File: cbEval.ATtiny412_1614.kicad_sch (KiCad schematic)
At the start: 59 parts, among them J1 Bergstik-II_3, J11 Bergstik-II_3, J12 Bergstik-II_3, J13 Bergstik-II_6, J14 Bergstik-II_6, J15 Bergstik-II_6, J16 Bergstik-II_3, J17 Bergstik-II_6, J18 Bergstik-II_3, J19 Bergstik-II_6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

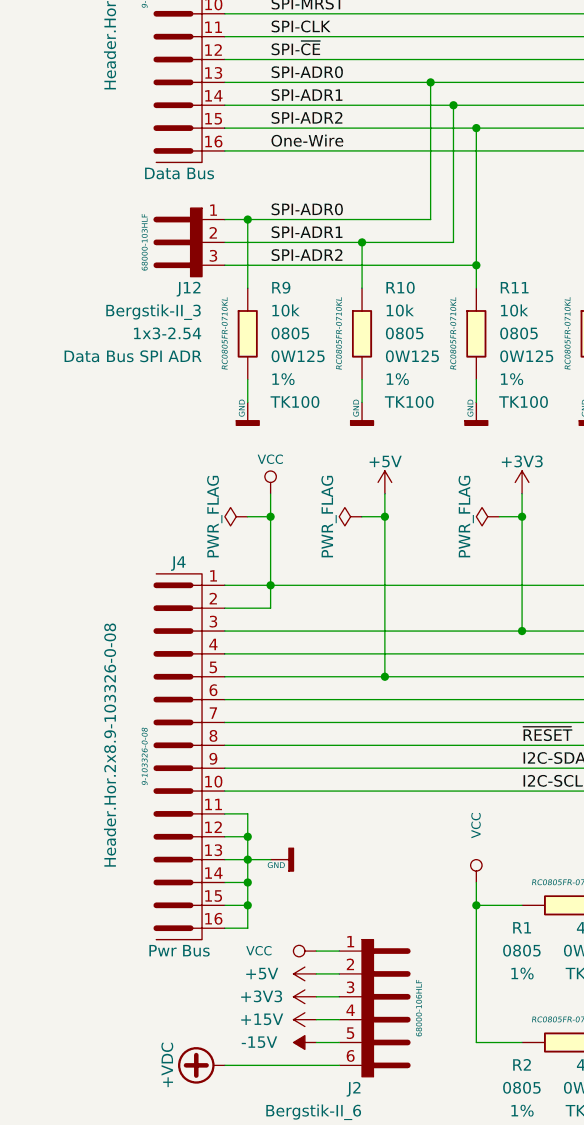
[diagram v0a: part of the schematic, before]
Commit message: Leiterplatte verkleinert, SilkScreen einiger Stecker verändert
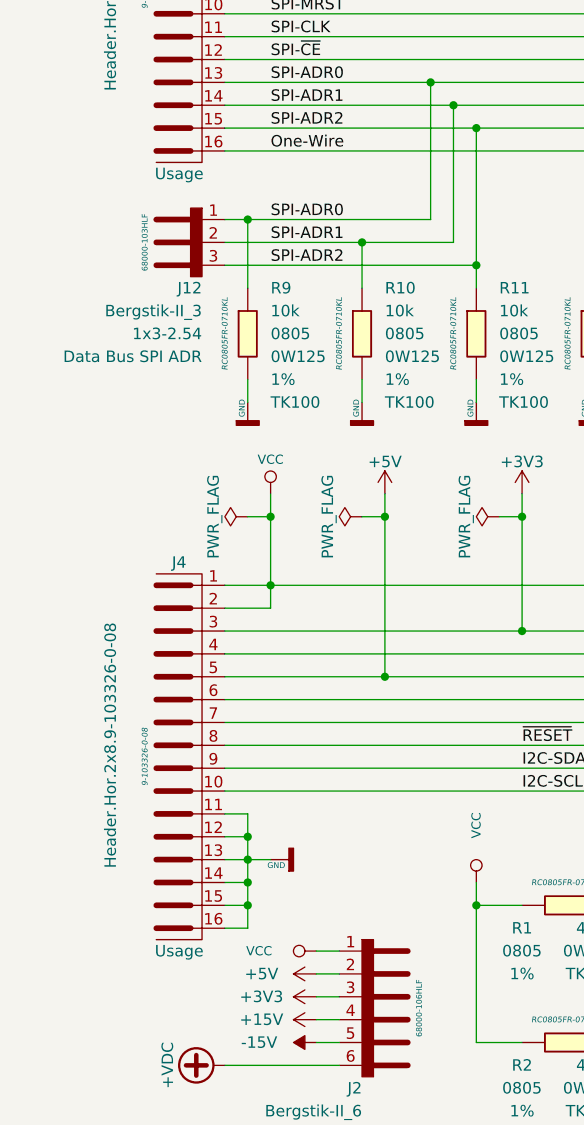
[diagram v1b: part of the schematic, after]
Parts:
- J3: footprint Connector_PinHeader_2.54mm:PinHeader_2x08_P2.54mm_Horizontal -> BTech.PinHeader.2-54mm:PinHeader_2x08_P2.54mm_Horizontal; Usage Data Bus -> Usage
- J4: footprint Connector_PinHeader_2.54mm:PinHeader_2x08_P2.54mm_Horizontal -> BTech.PinHeader.2-54mm:PinHeader_2x08_P2.54mm_Horizontal; Usage Pwr Bus -> Usage
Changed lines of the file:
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@@
     (property "Reference" "J4" (id 0) (at 27.94 129.54 0))
     (property "Value" "Header.Hor.2x8.9-103326-0-08" (id 1) (at 20.32 149.86 90))
-    (property "Footprint" "Connector_PinHeader_2.54mm:PinHeader_2x08_P2.54mm_Horizontal" (id 2) (at 17.78 149.86 90)
+    (property "Footprint" "BTech.PinHeader.2-54mm:PinHeader_2x08_P2.54mm_Horizontal" (id 2) (at 17.78 149.86 90)
       (effects (font (size 1.016 1.016)) hide)
     )
@@
       (effects (font (size 1.016 1.016)) hide)
     )
-    (property "Usage" "Pwr Bus" (id 4) (at 27.94 172.72 0))
+    (property "Usage" "Usage" (id 4) (at 27.94 172.72 0))
     (property "ID" "9-103326-0-08" (id 5) (at 24.13 151.13 90)
       (effects (font (size 0.635 0.635) italic))
@@
     (pin "1")
   )
-  (symbol (lib_id "J.AMPMODU-ModII:Header.Hor.2x8.9-103326-0-08") (at 30.48 63.5 0) (mirror y) (unit 1)
+  (symbol (lib_name "Header.Hor.2x8.9-103326-0-08_1") (lib_id "J.AMPMODU-ModII:Header.Hor.2x8.9-103326-0-08") (at 30.48 63.5 0) (mirror y) (unit 1)
     (in_bom yes) (on_board yes)
     (property "Reference" "J3" (id 0) (at 27.94 43.18 0))
     (property "Value" "Header.Hor.2x8.9-103326-0-08" (id 1) (at 20.32 63.5 90))
-    (property "Footprint" "Connector_PinHeader_2.54mm:PinHeader_2x08_P2.54mm_Horizontal" (id 2) (at 17.78 63.5 90)
+    (property "Footprint" "BTech.PinHeader.2-54mm:PinHeader_2x08_P2.54mm_Horizontal" (id 2) (at 17.78 63.5 90)
       (effects (font (size 1.016 1.016)) hide)
     )
@@
       (effects (font (size 1.016 1.016)) hide)
     )
-    (property "Usage" "Data Bus" (id 4) (at 27.94 86.36 0))
+    (property "Usage" "Usage" (id 4) (at 27.94 86.36 0))
     (property "ID" "9-103326-0-08" (id 5) (at 24.13 64.77 90)
       (effects (font (size 0.635 0.635) italic))
@@
     )
     (path "/b3060ad3-f562-456c-b6a7-a7754cda5678"
-      (reference "J3") (unit 1) (value "Header.Hor.2x8.9-103326-0-08") (footprint "Connector_PinHeader_2.54mm:PinHeader_2x08_P2.54mm_Horizontal")
+      (reference "J3") (unit 1) (value "Header.Hor.2x8.9-103326-0-08") (footprint "BTech.PinHeader.2-54mm:PinHeader_2x08_P2.54mm_Horizontal")
     )
     (path "/47fc6a69-dbf0-45e5-a1c0-ed588626fbeb"
-      (reference "J4") (unit 1) (value "Header.Hor.2x8.9-103326-0-08") (footprint "Connector_PinHeader_2.54mm:PinHeader_2x08_P2.54mm_Horizontal")
+      (reference "J4") (unit 1) (value "Header.Hor.2x8.9-103326-0-08") (footprint "BTech.PinHeader.2-54mm:PinHeader_2x08_P2.54mm_Horizontal")
     )
     (path "/d76e15a9-b548-4883-8a79-3a3d54a6ee37"

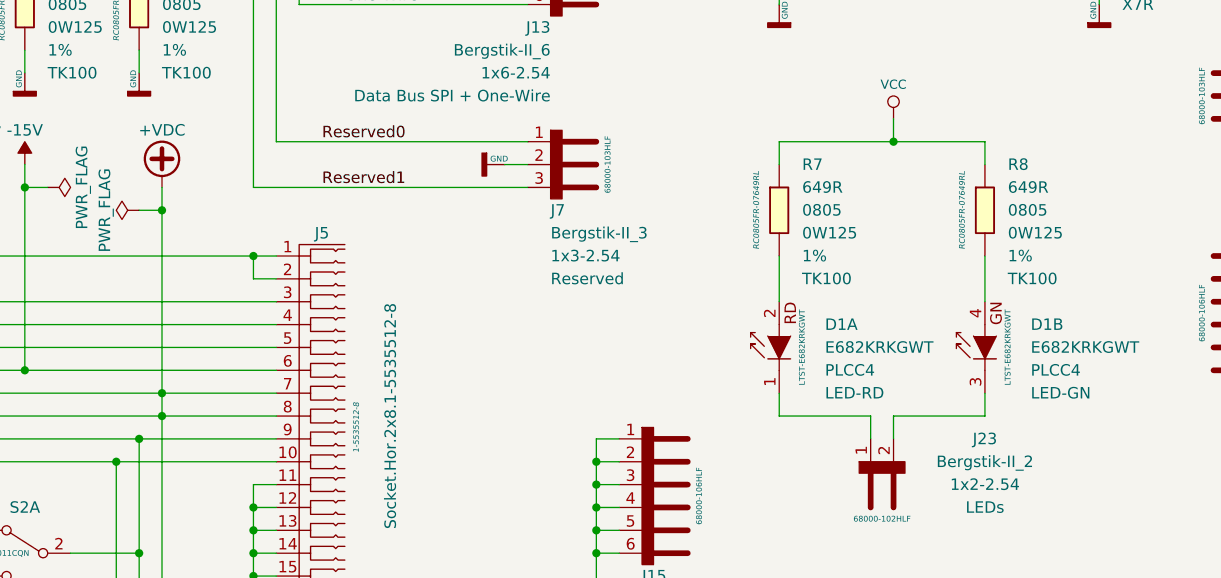
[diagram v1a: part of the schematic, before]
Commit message: Kurzschluss entfernt, Vorwiderstand für grüne LEDs auf 560 verringert
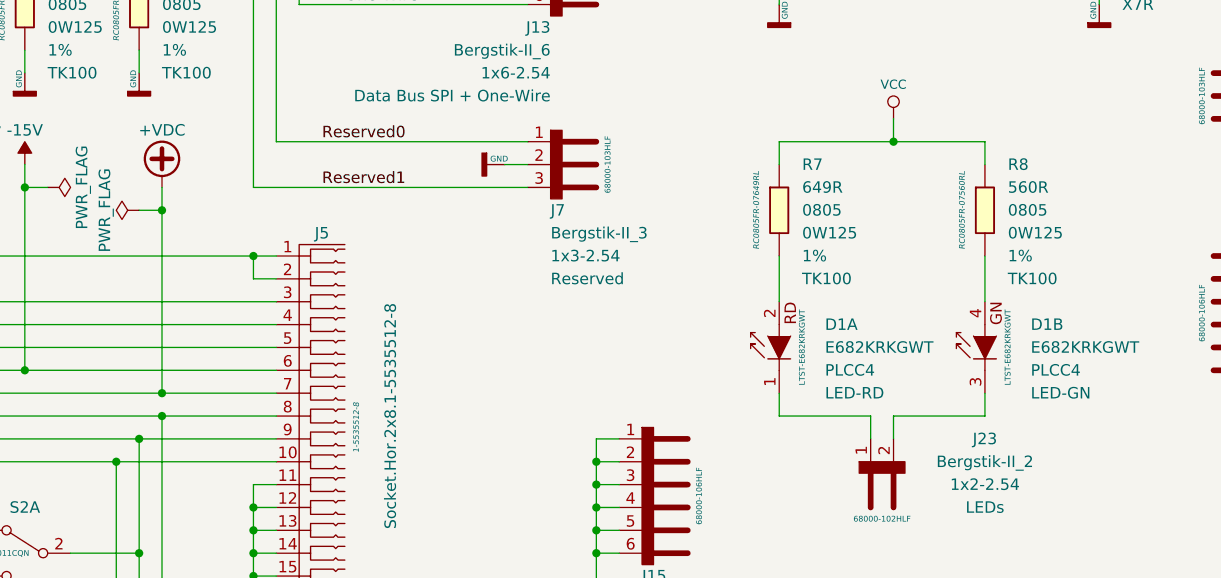
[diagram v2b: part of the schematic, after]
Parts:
- R8: value 649R -> 560R; symbol R.Yageo.RC0805:649R -> R.Yageo.RC0805:560R; ID RC0805FR-07649RL -> RC0805FR-07560RL
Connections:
- net +VDC: no longer J1.1 (A1), J4.8, J5.8
- new net ~{RESET}: J1.1 (A1), J4.8, J5.8
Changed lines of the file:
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@@
     (stroke (width 0) (type solid) (color 0 0 0 0))
   )
-  (wire (pts (xy 101.6 147.32) (xy 101.6 149.86))
-    (stroke (width 0) (type solid) (color 0 0 0 0))
-  )
   (wire (pts (xy 33.02 27.94) (xy 48.26 27.94))
     (stroke (width 0) (type solid) (color 0 0 0 0))
@@
     )
   )
-  (symbol (lib_id "R.Yageo.RC0805:649R") (at 193.04 127 0) (unit 1)
+  (symbol (lib_id "R.Yageo.RC0805:560R") (at 193.04 127 0) (unit 1)
     (in_bom yes) (on_board yes)
     (property "Reference" "R8" (id 0) (at 195.58 121.92 0)
       (effects (font (size 1.27 1.27)) (justify left))
     )
-    (property "Value" "649R" (id 1) (at 195.58 124.46 0)
+    (property "Value" "560R" (id 1) (at 195.58 124.46 0)
       (effects (font (size 1.27 1.27)) (justify left))
     )
@@
       (effects (font (size 1.27 1.27)) (justify left))
     )
-    (property "ID" "RC0805FR-07649RL" (id 8) (at 190.5 127 90)
+    (property "ID" "RC0805FR-07560RL" (id 8) (at 190.5 127 90)
       (effects (font (size 0.635 0.635) italic))
     )
@@
     (pin "1")
   )
-  (symbol (lib_name "Header.Hor.2x8.9-103326-0-08_1") (lib_id "J.AMPMODU-ModII:Header.Hor.2x8.9-103326-0-08") (at 30.48 63.5 0) (mirror y) (unit 1)
+  (symbol (lib_id "J.AMPMODU-ModII:Header.Hor.2x8.9-103326-0-08") (at 30.48 63.5 0) (mirror y) (unit 1)
     (in_bom yes) (on_board yes)
     (property "Reference" "J3" (id 0) (at 27.94 43.18 0))
@@
     )
     (path "/5c5c76a2-e9a1-4ab2-95ed-b3824f4e16eb"
-      (reference "R8") (unit 1) (value "649R") (footprint "Resistor_SMD:R_0805_2012Metric")
+      (reference "R8") (unit 1) (value "560R") (footprint "Resistor_SMD:R_0805_2012Metric")
     )
     (path "/14f7267c-bcb9-4012-a902-1623c71f1c0f"
